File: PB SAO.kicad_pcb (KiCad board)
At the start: 2 copper layers, 52 x 150.4 mm, 15 parts, among them P1 SAO_1

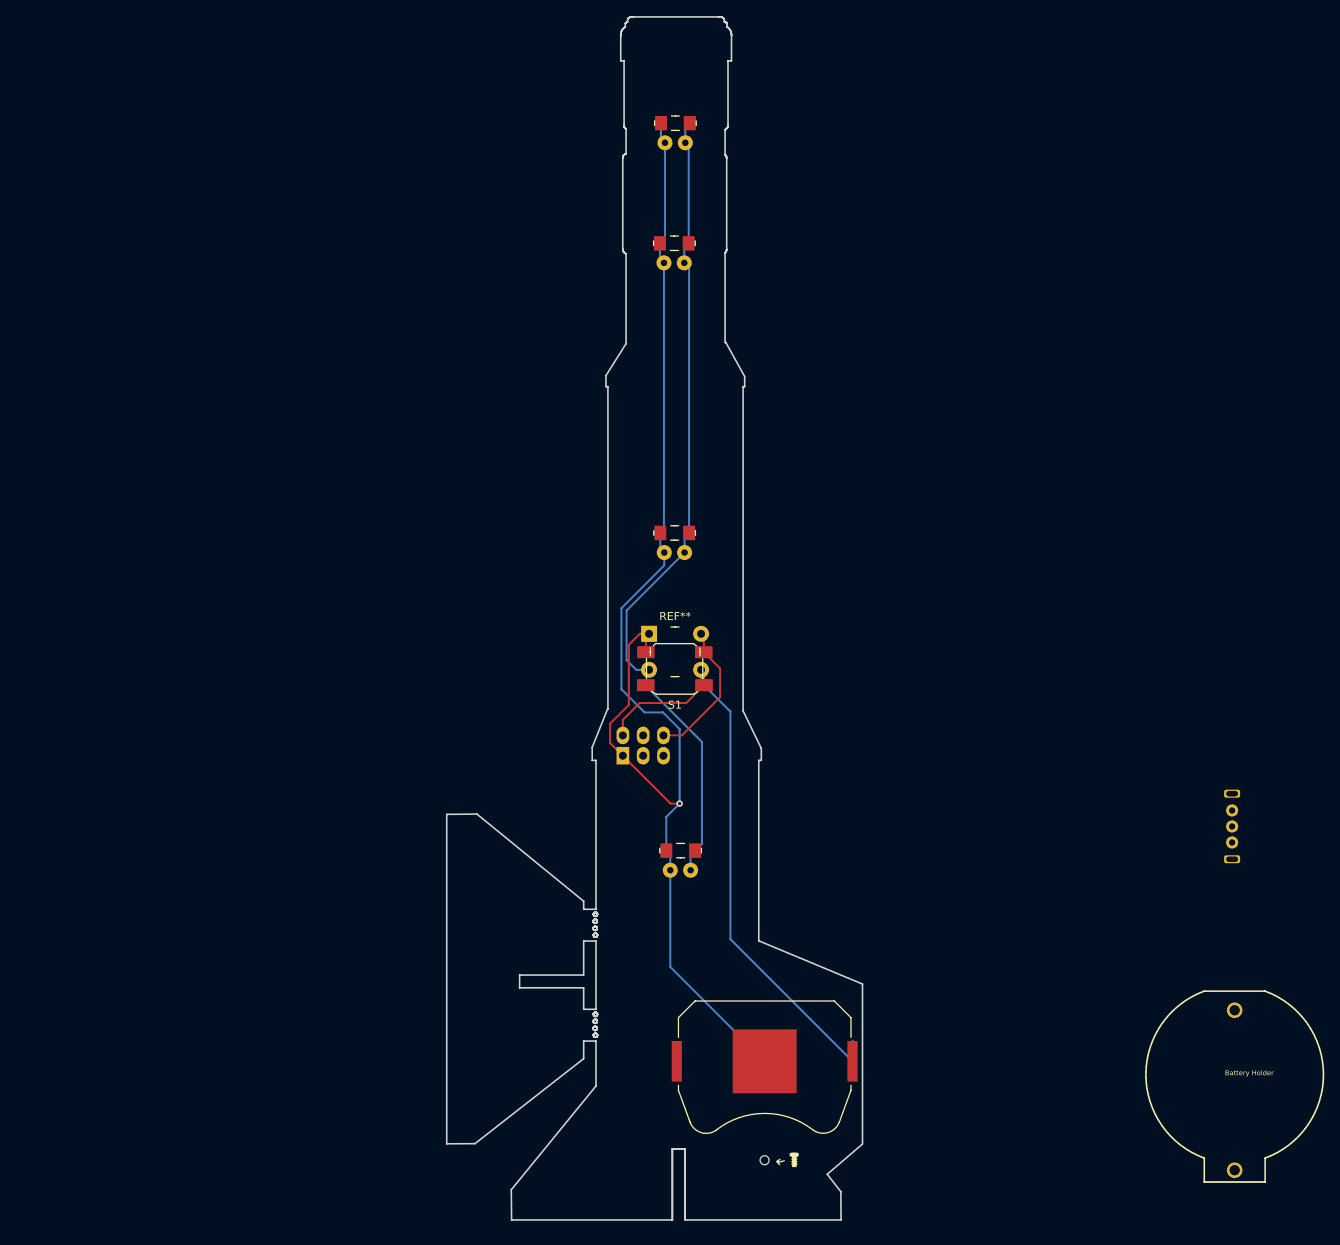
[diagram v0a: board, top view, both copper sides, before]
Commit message: Tidy up and schematic
Edge cuts are now symetrical.
Schematic created.
SAO or standalone mode.
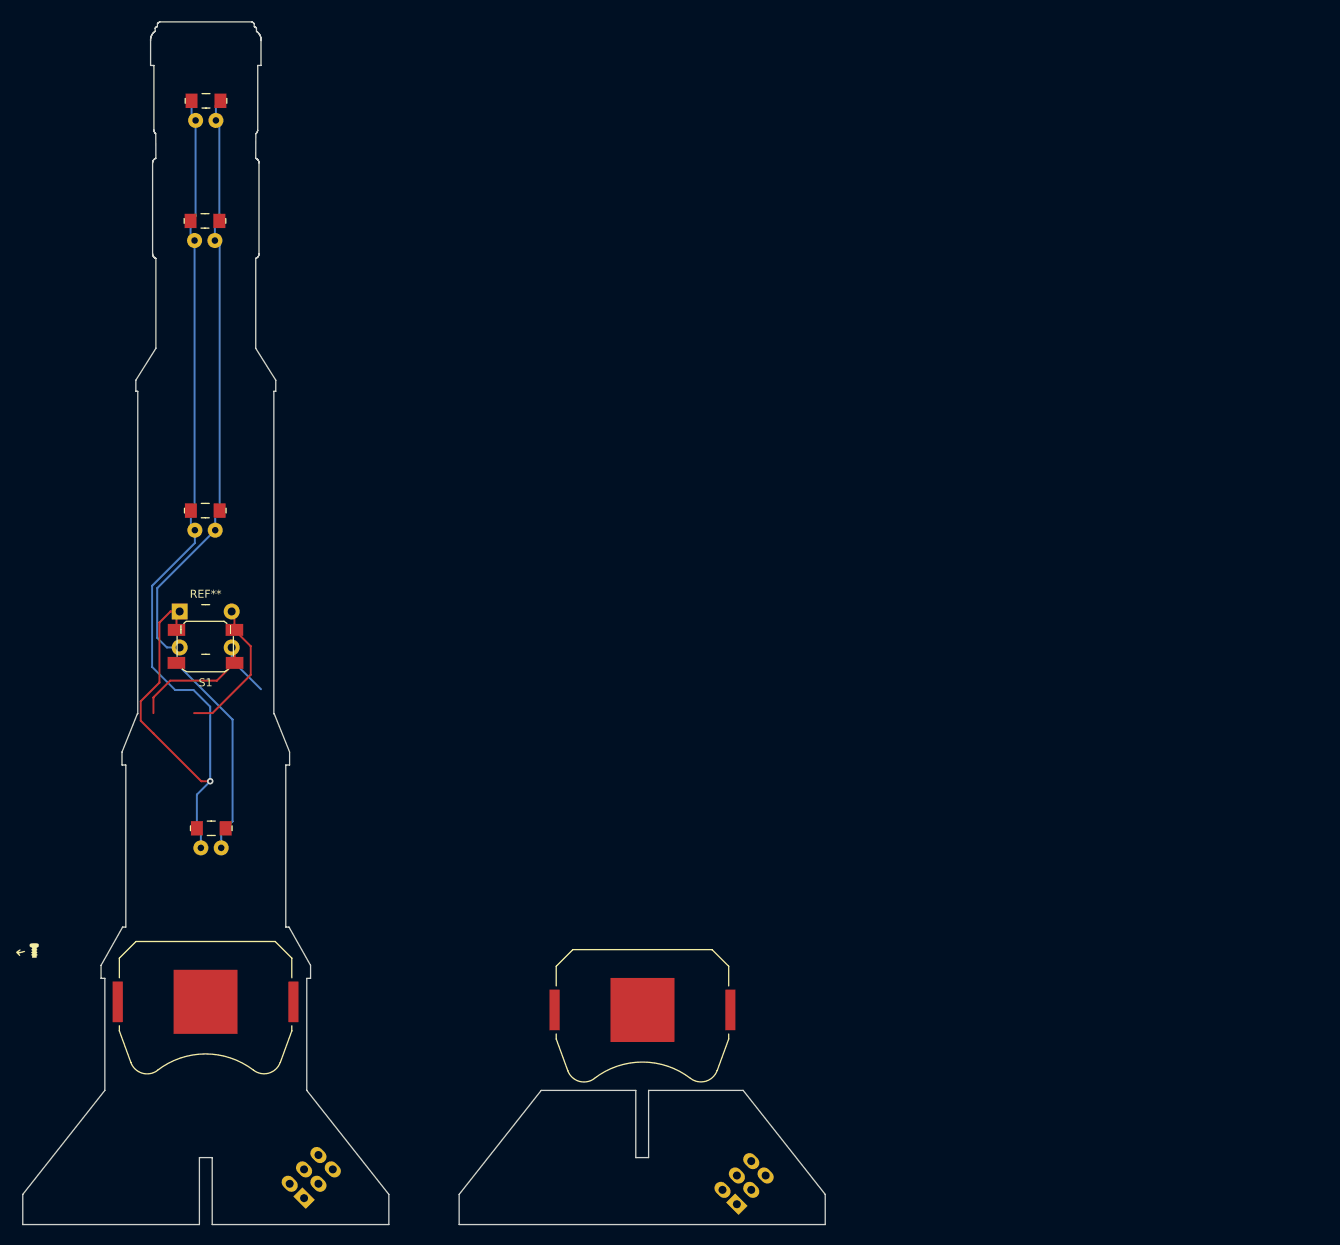
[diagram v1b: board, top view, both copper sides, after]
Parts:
- removed the >NAME at (148.5, 129.6)
- removed the >NAME at (147.8, 89.9)
- removed the >NAME at (147.7, 53.7)
- removed the REF** at (148.5, 127.2)
- removed the REF** at (147.8, 87.4)
- removed the REF** at (147.8, 51.2)
- removed Ref**: Battery Holder, adafruit:CoinCellBatt2032
- removed Slide Switch: SK12D07 Slide Switch Through Hole ELKEI, adafruit:SK12D07 Slide Switch Through Hole ELKEI
- added >NAME: >VALUE, adafruit:sidebendLED3MM, F.Cu at (89.8, 126.8)
- added >NAME: >VALUE, adafruit:sidebendLED3MM, F.Cu at (89.1, 87.1)
- added >NAME: >VALUE, adafruit:sidebendLED3MM, F.Cu at (89.0, 50.9)
- added BT1: BATTERY-20MM_SMD_4LEGS, BatteryHolder_Keystone_3034_1x20mm, F.Cu at (143.8, 147.1)
- added P1: SAO_1, adafruit:SAO_Header_6-Pin_Oval_AltPins, F.Cu at (156.5, 168.7)
- added REF**: 1206, digikey-footprints:1206, F.Cu at (89.9, 124.4)
- added REF**: 1206, digikey-footprints:1206, F.Cu at (89.1, 84.6)
- added REF**: 1206, digikey-footprints:1206, F.Cu at (89.1, 48.4)
- moved G*** 98.5 mm to (41.9, 146.1)
- moved BT1 70.3 mm to (89.2, 146.1)
- moved P1 68.0 mm to (102.4, 167.9), turned to 45 degrees
- moved S1 58.7 mm to (89.1, 105.6)
- moved REF** 58.7 mm to (85.9, 97.3)
- moved >NAME 58.7 mm to (89.2, 35.9)
- moved REF** 58.7 mm to (89.2, 33.4)
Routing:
- net (no net): track 355.8 -> 274.4 mm
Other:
- board size 52 x 150.4 mm -> 100.3 x 150.3 mm

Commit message: Updated footprints
Dual footprints.
Updated edge cuts
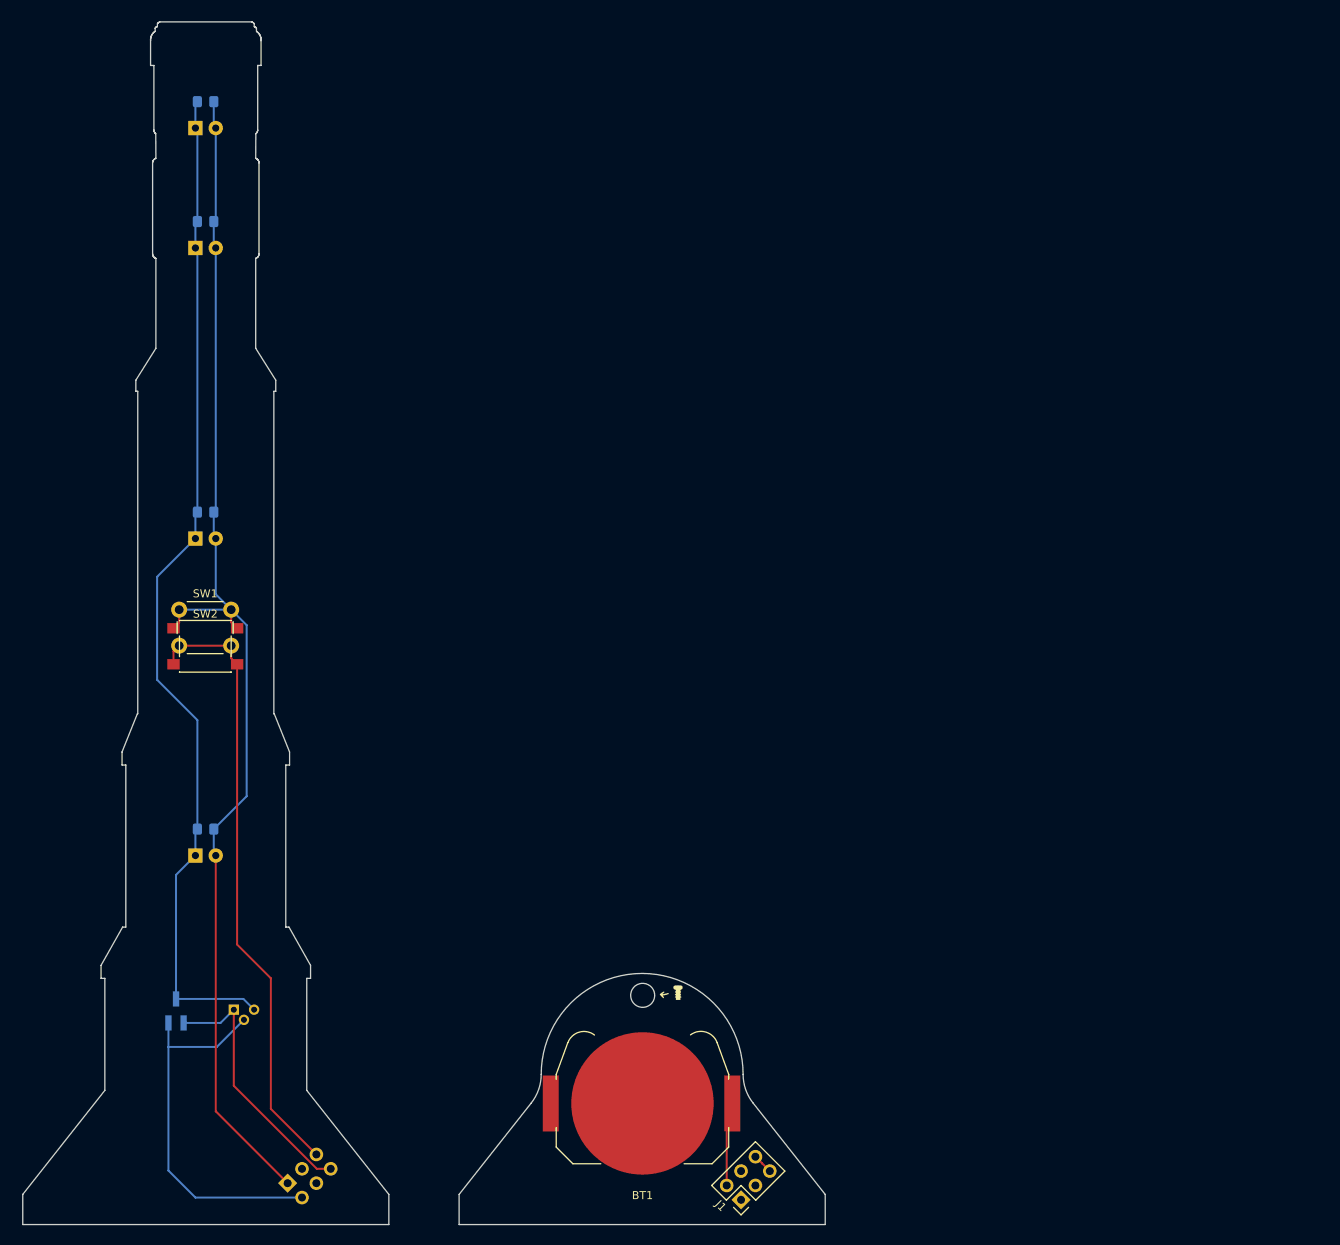
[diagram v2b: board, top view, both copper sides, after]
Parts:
- removed >NAME (x4): >VALUE, adafruit:sidebendLED3MM
- removed the BT1 at (143.8, 147.1)
- removed the BT1 at (89.2, 146.1)
- removed P1 (x2): SAO_1, adafruit:SAO_Header_6-Pin_Oval_AltPins
- removed REF** (x4): 1206, digikey-footprints:1206
- removed REF**: Switch_Tactile_THT_6x6mm_MJTP1230, digikey-footprints:Switch_Tactile_THT_6x6mm_MJTP1230
- removed S1: SMDButton4x4x1.5elkei, adafruit:SMDButton4x4x1.5elkei
- added BT1: CR2032, Battery:BatteryHolder_Keystone_3034_1x20mm, F.Cu at (143.8, 158.8)
- added D1: LED, LED_SMD:LED_0805_2012Metric_Pad1.15x1.40mm_HandSolder, B.Cu at (89.2, 33.5)
- added D2: LED, LED_SMD:LED_0805_2012Metric_Pad1.15x1.40mm_HandSolder, B.Cu at (89.2, 48.5)
- added D3: LED, LED_SMD:LED_0805_2012Metric_Pad1.15x1.40mm_HandSolder, B.Cu at (89.2, 84.8)
- added D4: LED, LED_SMD:LED_0805_2012Metric_Pad1.15x1.40mm_HandSolder, B.Cu at (89.2, 124.5)
- added D5: LED, LED_THT:LED_D3.0mm, B.Cu at (87.9, 36.8)
- added D6: LED, LED_THT:LED_D3.0mm, B.Cu at (87.9, 51.8)
- added D7: LED, LED_THT:LED_D3.0mm, B.Cu at (87.9, 88.1)
- added D8: LED, LED_THT:LED_D3.0mm, B.Cu at (87.9, 127.8)
- added H1: MountingHole, MountingHole:MountingHole_3mm, F.Cu at (143.8, 145.2)
- added J1: SAO_F, Connector_PinHeader_2.54mm:PinHeader_2x03_P2.54mm_Vertical, F.Cu at (156.1, 170.8)
- added J2: SAO_F, Connector_PinHeader_2.54mm:PinHeader_2x03_P2.54mm_Vertical, B.Cu at (99.4, 168.7)
- added Q1: 2N7002, Package_TO_SOT_SMD:SOT-23_Handsoldering, B.Cu at (85.5, 147.2)
- added Q2: 2N7002, Package_TO_SOT_THT:TO-92, B.Cu at (92.7, 147.0)
- added SW1: SW_Push, Button_Switch_THT:SW_PUSH_6mm, F.Cu at (85.9, 97.0)
- added SW2: SW_Push, Button_Switch_SMD:SW_Push_1P1T_NO_6x6mm_H9.5mm, F.Cu at (89.1, 101.6)
- moved G*** 80.6 mm to (122.4, 151.3)
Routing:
- net (no net): track 274.4 -> 0.00 mm, vias 1 -> 0
- net /VCC: track 0.00 -> 154.6 mm
- net Net-(D1-Pad1): track 0.00 -> 128.2 mm
- net Net-(J2-Pad5): track 0.00 -> 77.1 mm
- net GND: track 0.00 -> 47.4 mm
- net /IO_high: track 0.00 -> 32.9 mm
- net +3V3: track 0.00 -> 10.4 mm
- net Net-(J1-Pad5): track 0.00 -> 2.54 mm
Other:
- outline, holes or cut-outs redrawn

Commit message: Updated position of connectors
battery connector needed to be moved.
traces are thicker.
Rounded tracks version added (alternative kicad_pcb)
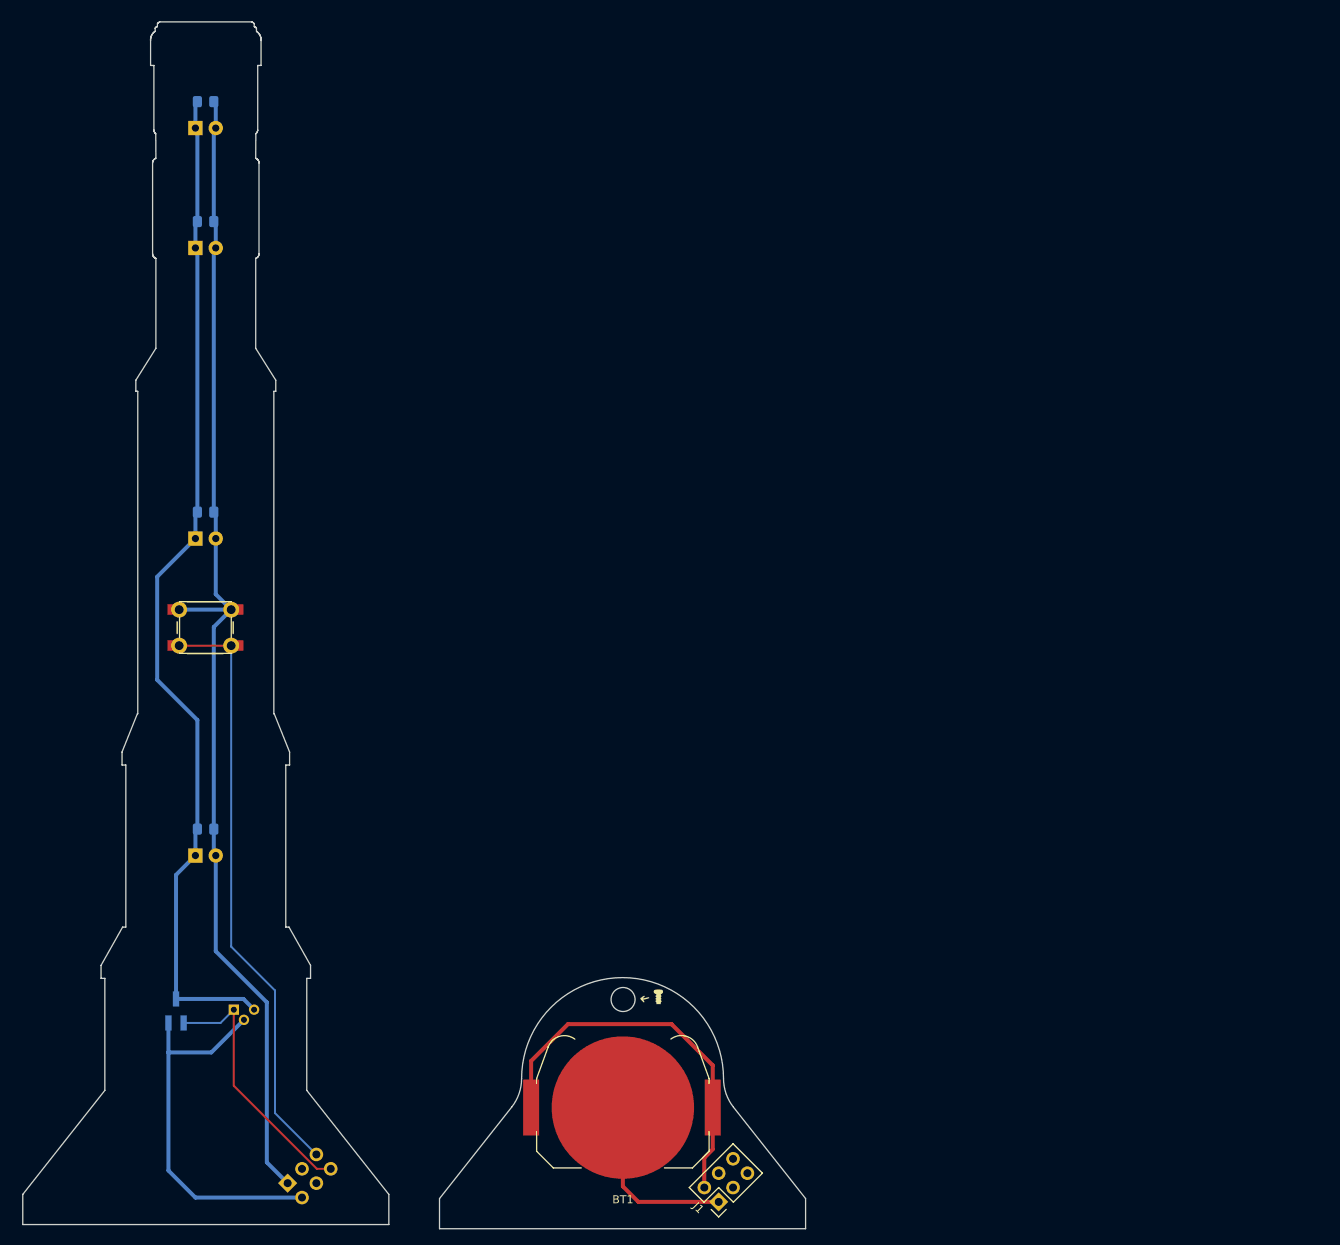
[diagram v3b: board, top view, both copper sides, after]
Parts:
- moved J1 2.81 mm to (153.3, 171.1)
- moved BT1 2.50 mm to (141.3, 159.3)
- moved G*** 2.50 mm to (119.9, 151.8)
- moved H1 2.50 mm to (141.3, 145.8)
- moved SW2 2.35 mm to (89.1, 99.3)
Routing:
- net +3V3: track 10.4 -> 48.9 mm
- net GND: track 47.4 -> 70.3 mm
- net /VCC: track 154.6 -> 148.1 mm
- net Net-(J2-Pad5): track 77.1 -> 74.5 mm
- net Net-(J1-Pad5): track 2.54 -> 0.00 mm
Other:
- board size 100.3 x 150.3 mm -> 97.9 x 150.9 mm

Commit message: Fixed up a few connections
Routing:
- net Net-(J1-Pad5): track 0.00 -> 2.54 mm
